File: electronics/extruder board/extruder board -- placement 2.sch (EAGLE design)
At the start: 20 parts, among them IC1 MAX6675, IC2 MAX6675

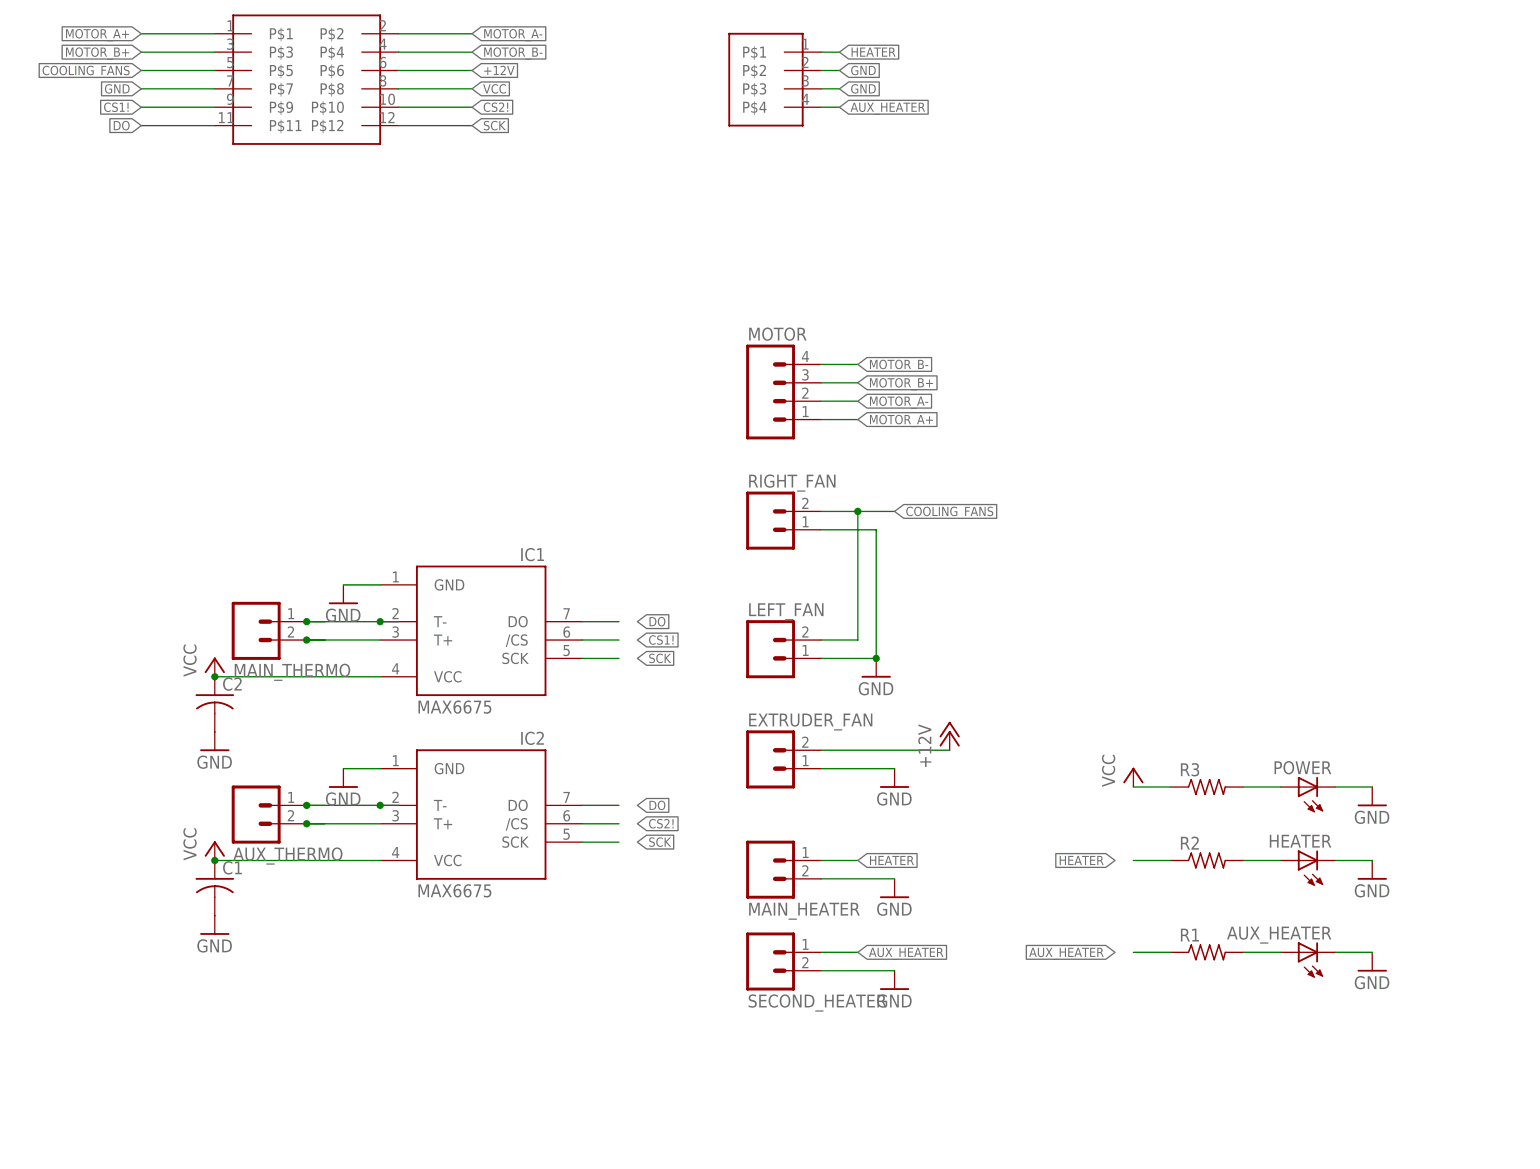
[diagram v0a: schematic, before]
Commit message: Updated extruder board V1.1
-Changed pin assignment on connectors
-fixed bugs on Left / Right Fan
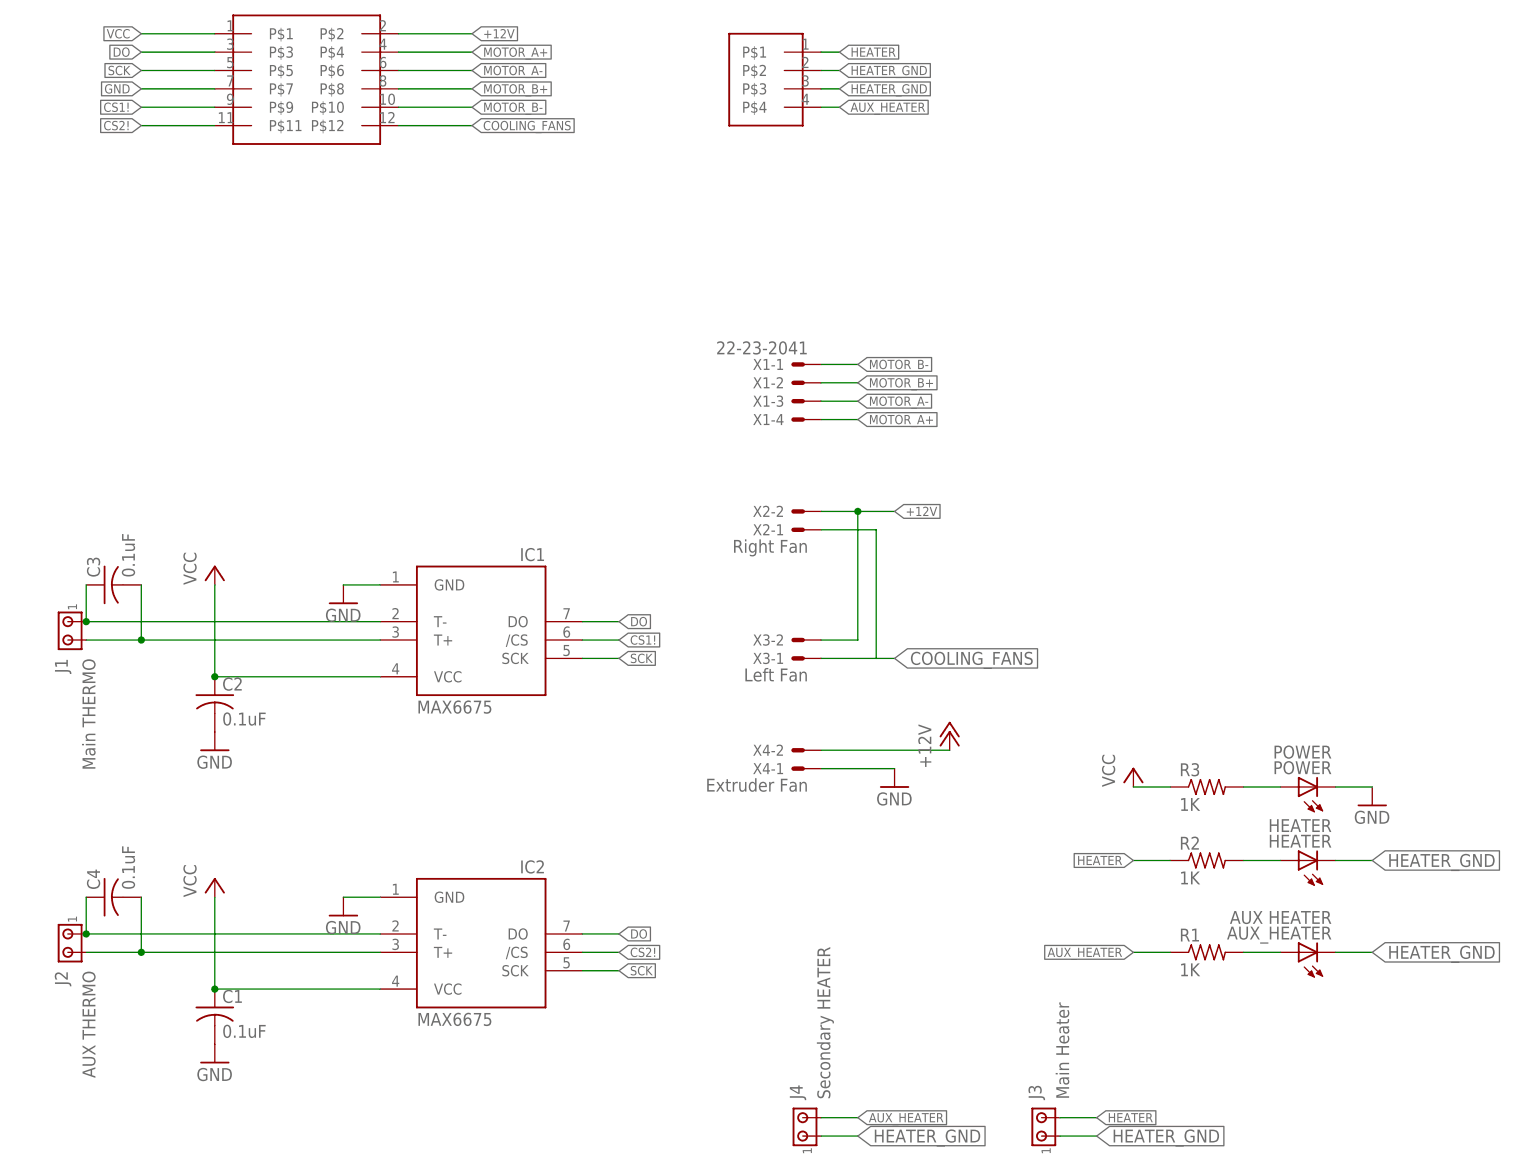
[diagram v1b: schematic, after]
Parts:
- removed AUX_THERMO, MAIN_HEATER, MAIN_THERMO, SECOND_HEATER: M023.5MM_LOCK, SparkFun-Connectors:M023.5MM_LOCK
- removed EXTRUDER_FAN: M02POLAR_LOCK, extruder board -- placement 2:M02POLAR_LOCK
- removed LEFT_FAN, RIGHT_FAN: M02JST-PTH-2, extruder board -- placement 2:M02JST-PTH-2
- removed MOTOR: (no value), extruder board -- placement 2:M04POLAR_LOCK
- added C3, C4: 0.1uF, rcl:C-USC0603
- added J1: Main THERMO, 555 delay toggle switch:CON-AMP_MTA02-156
- added J2: AUX THERMO, 555 delay toggle switch:CON-AMP_MTA02-156
- added J3: Main Heater, 555 delay toggle switch:CON-AMP_MTA02-156
- added J4: Secondary HEATER, 555 delay toggle switch:CON-AMP_MTA02-156
- added X1: 22-23-2041, con-molex:22-23-2041
- added X2: Right Fan, con-molex:22-23-2021
- added X3: Left Fan, con-molex:22-23-2021
- added X4: Extruder Fan, con-molex:22-23-2021
- AUX_HEATER: value (none) -> AUX HEATER
- C1, C2: value (none) -> 0.1uF
- HEATER: value (none) -> HEATER
- POWER: value (none) -> POWER
- R1, R2, R3: value (none) -> 1K
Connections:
- new net HEATER_GND: AUX_HEATER.C, HEATER.C, J3.1, J4.1, U$3.P$2, U$3.P$3
- net +12V: now also U$1.P$2, X2-2.S, X3-2.S, X4-2.S; no longer EXTRUDER_FAN.2, U$1.P$6
- net AUX_HEATER: now also J4.2; no longer SECOND_HEATER.1
- net COOLING_FANS: now also U$1.P$12, X2-1.S, X3-1.S; no longer LEFT_FAN.2, RIGHT_FAN.2, U$1.P$5
- net CS2!: now also U$1.P$11; no longer U$1.P$10
- net DO: now also U$1.P$3; no longer U$1.P$11
- net GND: now also X4-1.S; no longer AUX_HEATER.C, EXTRUDER_FAN.1, HEATER.C, LEFT_FAN.1, MAIN_HEATER.2, RIGHT_FAN.1, SECOND_HEATER.2, U$3.P$2, U$3.P$3
- net HEATER: now also J3.2; no longer MAIN_HEATER.1
- net MOTOR_A+: now also U$1.P$4, X1-4.S; no longer MOTOR.1, U$1.P$1
- net MOTOR_A-: now also U$1.P$6, X1-3.S; no longer MOTOR.2, U$1.P$2
- net MOTOR_B+: now also U$1.P$8, X1-2.S; no longer MOTOR.3, U$1.P$3
- net MOTOR_B-: now also U$1.P$10, X1-1.S; no longer MOTOR.4, U$1.P$4
- net N$1: now also C4.1, IC2.T-, J2.1; no longer IC1.T+, MAIN_THERMO.2
- net N$2: now also C3.1, J1.1; no longer MAIN_THERMO.1
- net N$3: now also C3.2, IC1.T+, J1.2; no longer AUX_THERMO.2, IC2.T+
- net N$4: now also C4.2, IC2.T+, J2.2; no longer AUX_THERMO.1, IC2.T-
- net SCK: now also U$1.P$5; no longer U$1.P$12
- net VCC: now also U$1.P$1; no longer U$1.P$8
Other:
- moved on the sheet: C1, IC2
